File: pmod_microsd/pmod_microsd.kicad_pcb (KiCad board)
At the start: 2 copper layers, 11 parts, among them J1 PZ254R-12-12P, J2 Micro_SD_Card_Det2

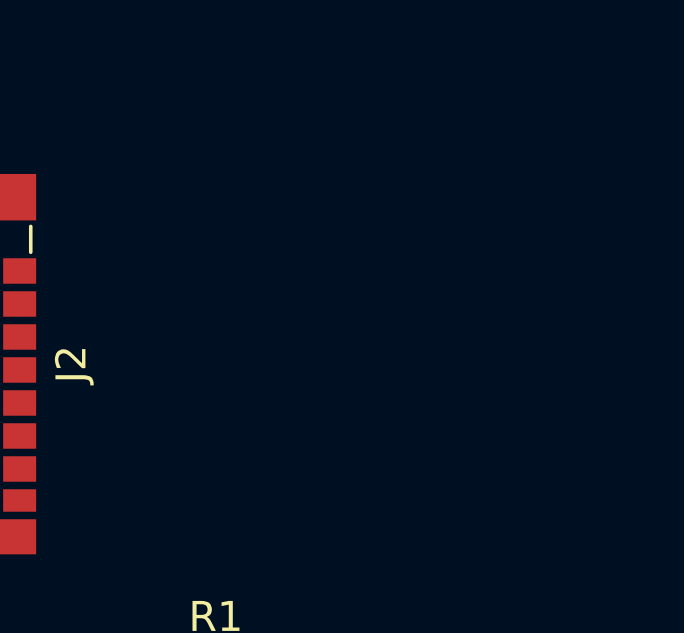
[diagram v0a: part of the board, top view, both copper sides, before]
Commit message: pmod_microsd/*.kicad_pcb: import schematic to pcb
- Import components from schematic to PCB

Signed-off-by: Huang Rui <vowstar@gmail.com>
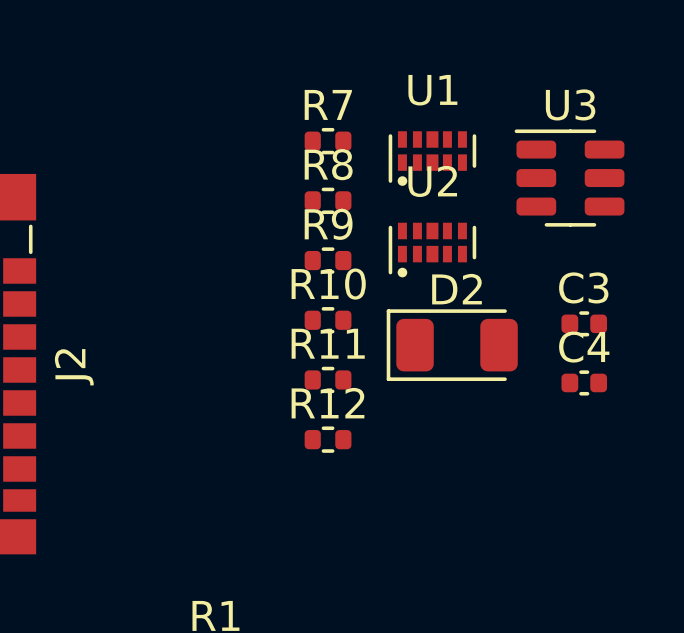
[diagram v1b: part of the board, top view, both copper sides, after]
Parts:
- added C3: 100n, Capacitor_SMD:C_0402_1005Metric, F.Cu at (134.0, 117.6)
- added C4: 100n, Capacitor_SMD:C_0402_1005Metric, F.Cu at (134.0, 119.6)
- added D2: NCD1206O1, LED_SMD:LED_1206_3216Metric, F.Cu at (129.8, 118.4)
- added R10: 10k, Resistor_SMD:R_0402_1005Metric, F.Cu at (125.5, 117.5)
- added R11: 6.8k, Resistor_SMD:R_0402_1005Metric, F.Cu at (125.5, 119.5)
- added R12: 6.8k, Resistor_SMD:R_0402_1005Metric, F.Cu at (125.5, 121.5)
- added R7: 330, Resistor_SMD:R_0402_1005Metric, F.Cu at (125.5, 111.6)
- added R8: 10k, Resistor_SMD:R_0402_1005Metric, F.Cu at (125.5, 113.5)
- added R9: 10k, Resistor_SMD:R_0402_1005Metric, F.Cu at (125.5, 115.5)
- added U1: RCLAMP0524P, CHIPSAlliance_Package_SON:USON-10_2.5x1.0mm_P0.5mm, F.Cu at (129.0, 111.9)
- added U2: RCLAMP0524P, CHIPSAlliance_Package_SON:USON-10_2.5x1.0mm_P0.5mm, F.Cu at (129.0, 114.9)
- added U3: AIP74LVC1T45GB236TR, Package_TO_SOT_SMD:SOT-23-6, F.Cu at (133.6, 112.8)
- C1, C2: value 100n -> 10u
- R1, R2: value 47k -> 200
- R3, R4, R5: value 47k -> 330
- R6: value 6.8k -> 330
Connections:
- C1 pad 1: VADJ -> 3P3V
- D1 pad 2: 3P3V -> Net-(D1-A)
- J1 pad 10: unconnected-(J1-Pin_10-Pad10) -> /SD_WP_PMOD
- J1 pad 9: /HVGPIO5 -> /SD_DET_PMOD
- J2 pad 10: Net-(J2-DET_A) -> /SD_DET
- R1 pad 1: /SD_DAT0 -> /SD_DET
- R1 pad 2: Net-(R1-Pad2) -> /SD_DET_PMOD
- R2 pad 1: /SD_DAT1 -> /SD_WP
- R2 pad 2: Net-(R1-Pad2) -> /SD_WP_PMOD
- R3 pad 1: /SD_DAT2 -> /SD_DAT0
- R3 pad 2: Net-(R1-Pad2) -> 3P3V
- R4 pad 1: /SD_DAT3 -> /SD_DAT1
- R4 pad 2: Net-(R1-Pad2) -> 3P3V
- R5 pad 1: /SD_CMD -> /SD_DAT2
- R5 pad 2: Net-(R1-Pad2) -> 3P3V
- R6 pad 1: Net-(J2-DET_A) -> /SD_DAT3
- R6 pad 2: Net-(D1-K) -> 3P3V

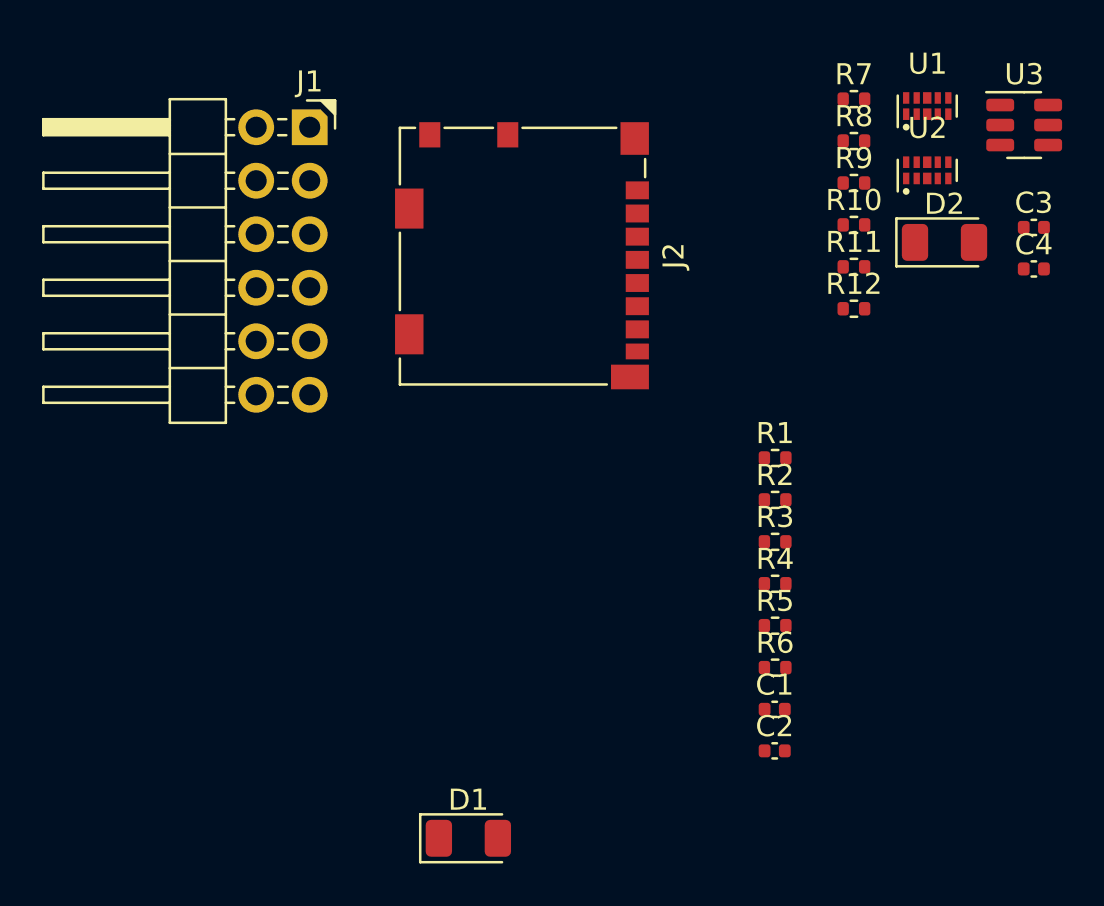
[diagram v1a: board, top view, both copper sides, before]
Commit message: pmod_microsd/*.kicad_pcb: draft placement
- Preliminary completion of component placement draft

Signed-off-by: Huang Rui <vowstar@gmail.com>
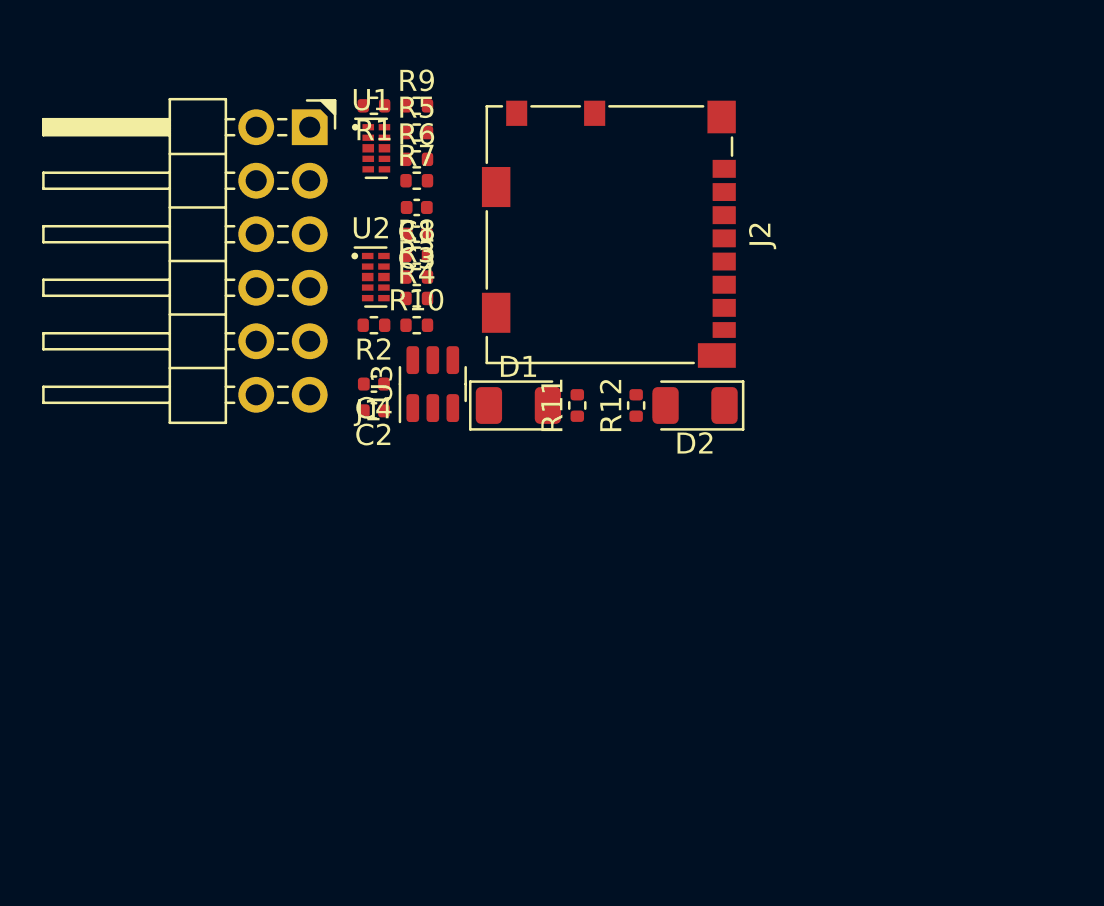
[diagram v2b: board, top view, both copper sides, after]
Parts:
- moved C4 31.8 mm to (102.7, 125.1), turned to 180 degrees
- moved U3 30.6 mm to (105.5, 125.1), turned to 90 degrees
- moved R6 29.5 mm to (104.7, 114.4)
- moved C3 29.3 mm to (104.7, 118.0), turned to 180 degrees
- moved C1 29.3 mm to (104.7, 116.7), turned to 180 degrees
- moved R5 28.9 mm to (104.7, 113.1)
- moved U2 26.7 mm to (102.8, 120.0), turned to -90 degrees
- moved U1 26.2 mm to (102.8, 113.9), turned to -90 degrees
- moved R1 25.3 mm to (102.7, 111.9), turned to 180 degrees
- moved C2 24.9 mm to (102.7, 126.4), turned to 180 degrees
- moved R4 21.7 mm to (104.7, 121.0)
- moved R8 21.5 mm to (104.7, 119.0)
- moved R10 21.3 mm to (104.7, 122.3)
- moved R3 21.1 mm to (104.7, 120.0)
- moved R7 21.1 mm to (104.7, 115.4)
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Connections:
- U1 pad 1: /SD_DAT3 -> /SD_DET_PMOD
- U1 pad 10: /SD_DAT3 -> /SD_DET_PMOD
- U1 pad 2: /SD_CMD -> /SD_DAT2
- U1 pad 4: /SD_DAT0 -> /SD_DAT3
- U1 pad 5: /SD_CLK -> /SD_CMD
- U1 pad 6: /SD_CLK -> /SD_CMD
- U1 pad 7: /SD_DAT0 -> /SD_DAT3
- U1 pad 9: /SD_CMD -> /SD_DAT2
- U2 pad 1: /SD_DAT1 -> /SD_CLK
- U2 pad 10: /SD_DAT1 -> /SD_CLK
- U2 pad 2: /SD_DAT2 -> /SD_DAT0
- U2 pad 4: /SD_DET_PMOD -> /SD_DAT1
- U2 pad 7: /SD_DET_PMOD -> /SD_DAT1
- U2 pad 9: /SD_DAT2 -> /SD_DAT0

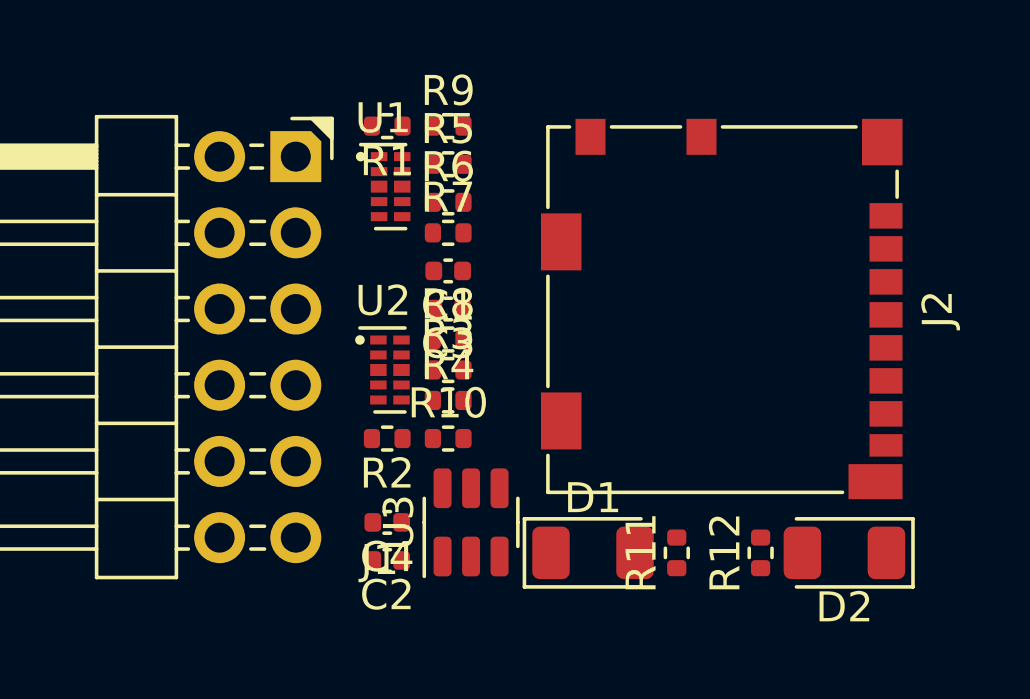
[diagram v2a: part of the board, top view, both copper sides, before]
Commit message: pmod_microsd/*.kicad_pcb: PCB outline definition
- Complete PCB outline and size definition
- Arrange silk screen
- Arrange text objects

Signed-off-by: Huang Rui <vowstar@gmail.com>
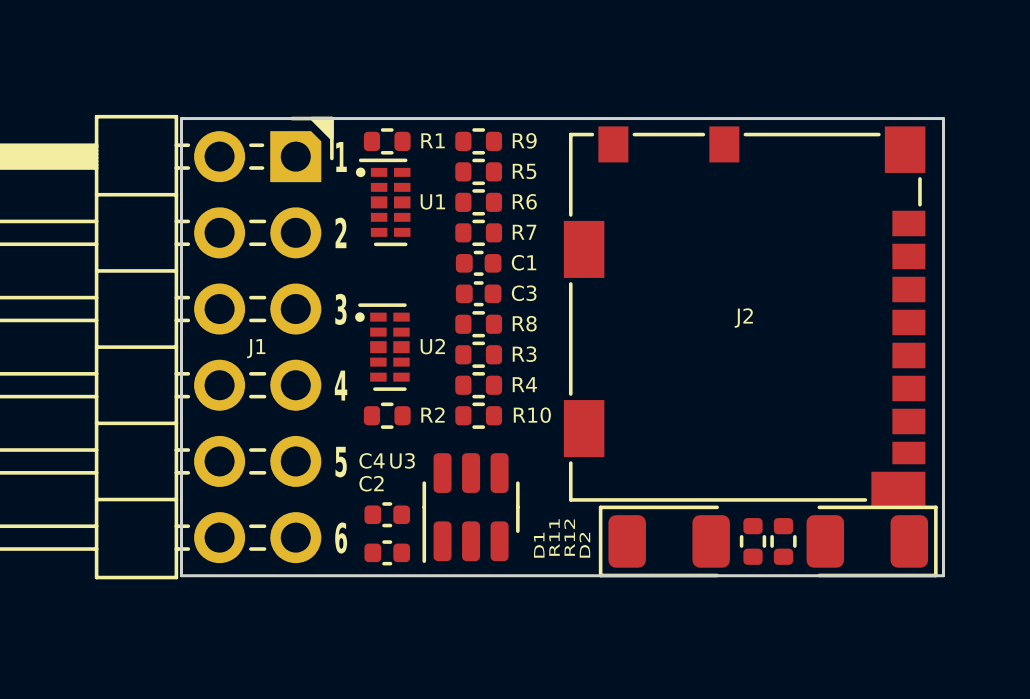
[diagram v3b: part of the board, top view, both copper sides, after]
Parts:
- moved D1 2.57 mm to (112.1, 125.7)
- moved R11 2.57 mm to (114.9, 125.7)
- moved R10 1.27 mm to (105.7, 121.5)
- moved R3 1.14 mm to (105.7, 119.5)
- moved C3 1.14 mm to (105.7, 117.5)
- moved R4 1.14 mm to (105.7, 120.5)
- moved R8 1.14 mm to (105.7, 118.5)
- moved R9 1.14 mm to (105.7, 112.4)
- moved C1 1.05 mm to (105.7, 116.4)
- moved R5 1.05 mm to (105.7, 113.4)
- moved R6 1.02 mm to (105.7, 114.4)
- moved R7 1.02 mm to (105.7, 115.4)
- moved D2 0.85 mm to (118.7, 125.7)
- moved R12 0.85 mm to (115.9, 125.7)
- moved J2 0.80 mm to (114.6, 118.2)
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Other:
- board outline added: 25.4 x 15.2 mm
- board text added: "1"
- board text added: "2"
- board text added: "3"
- board text added: "4"
- board text added: "5"
- board text added: "6"

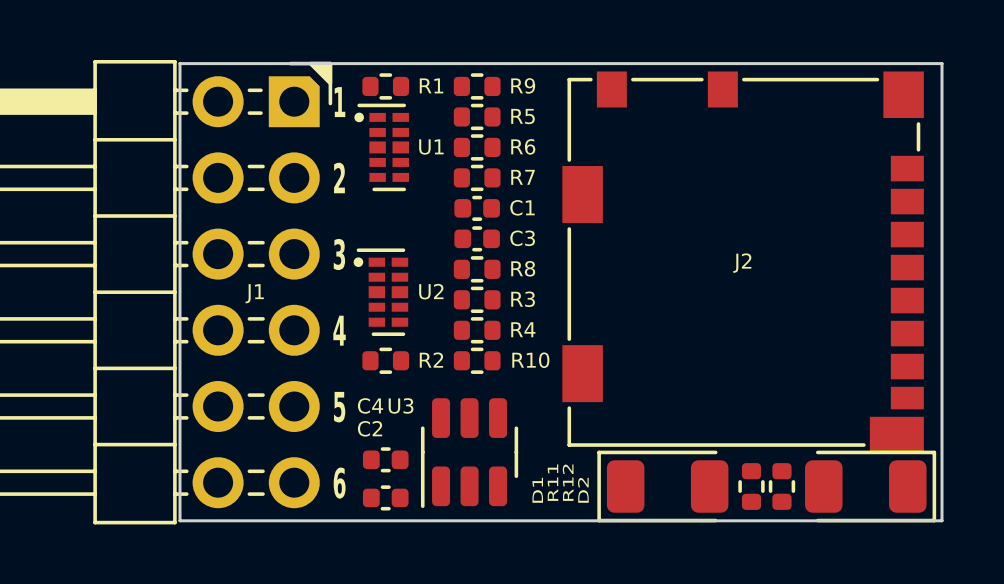
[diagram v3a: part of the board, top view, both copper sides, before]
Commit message: pmod_microsd/*.kicad_pcb: Complete PCB layout and routing
- Complete PCB layout
- Complete PCB routing
- Complete PCB silk screen placement
- LVS comparison successful
- DRC cleared

Signed-off-by: Huang Rui <vowstar@gmail.com>
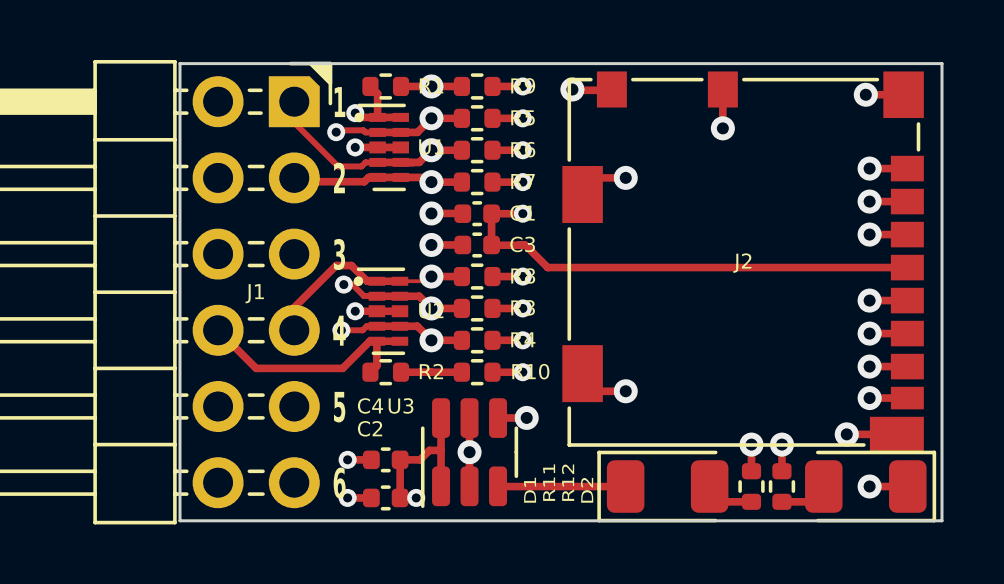
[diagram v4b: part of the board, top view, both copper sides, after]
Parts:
- moved U2 0.63 mm to (102.8, 119.9)
- moved R10 0.38 mm to (105.7, 121.9)
- moved R2 0.38 mm to (102.7, 121.9)
- moved R4 0.33 mm to (105.7, 120.8)
- moved R3 0.29 mm to (105.7, 119.8)
- moved R8 0.24 mm to (105.7, 118.7)
- moved C3 0.20 mm to (105.7, 117.7)
- moved C1 0.18 mm to (105.7, 116.6)
- moved R7 0.14 mm to (105.7, 115.6)
- moved R6 0.09 mm to (105.7, 114.5)
- turned R11 to -90 degrees
- turned R12 to -90 degrees
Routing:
- net 3P3V: track 0.00 -> 31.9 mm, vias 0 -> 12
- net /SD_DAT1: track 0.00 -> 30.7 mm, vias 0 -> 3
- net /SD_DAT2: track 0.00 -> 25.4 mm, vias 0 -> 3
- net /SD_DET: track 0.00 -> 24.6 mm, vias 0 -> 3
- net /SD_DAT3: track 0.00 -> 24.2 mm, vias 0 -> 2
- net /SD_CLK: track 0.00 -> 23.4 mm, vias 0 -> 2
- net /SD_DAT0: track 0.00 -> 23.0 mm, vias 0 -> 3
- net /SD_CMD: track 0.00 -> 22.4 mm, vias 0 -> 2
- net GND: track 0.00 -> 19.1 mm, vias 0 -> 14
- net /SD_DET_PMOD: track 0.00 -> 11.2 mm, vias 0 -> 1
- net /SD_WP_PMOD: track 0.00 -> 8.09 mm
- net Net-(D1-K): track 0.00 -> 4.26 mm
- net /SD_WP: track 0.00 -> 2.03 mm
- net Net-(D2-A): track 0.00 -> 1.61 mm
- net Net-(D1-A): track 0.00 -> 1.61 mm
- added copper zone on In2.Cu, net 3P3V
- added copper zone on B.Cu, net GND
- added copper zone on F.Cu, net GND
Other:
- copper layers 2 -> 4
- board text added: "CLK"
- board text added: "CMD"
- board text added: "D0"
- board text added: "D1"
- board text added: "D2"
- board text added: "D3"
- board text added: "GND"
- board text added: "PMOD_MICROSD Rev: ${REVISION} 6buE6ZSQ By: Rui Huang Date: ${ISSUE_DATE}"
- board text added: "VDD"
- board text added: "~{CD}"
- board text added: "~{WP}"

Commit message: pmod_microsd:*.kicad_pcb: add board characteristics
- Add board stackup table
- Add board characteristics

Signed-off-by: Huang Rui <vowstar@gmail.com>
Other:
- board text added: "0"
- board text added: "0 mm"
- board text added: "0.01 mm"
- board text added: "0.02"
- board text added: "0.035 mm"
- board text added: "0.1 mm"
- board text added: "0.1270 mm / 0.1270 mm"
- board text added: "0.3000 mm"
- board text added: "1.257 mm"
- board text added: "1.6170 mm"
- board text added: "2313"
- board text added: "25.4000 mm x 15.2400 mm"
- board text added: "3.3"
- board text added: "4.05"
- board text added: "4.5"
- board text added: "B.Cu"
- board text added: "B.Mask"
- board text added: "B.Paste"
- board text added: "B.Silkscreen"
- board text added: "BOARD CHARACTERISTICS"
- board text added: "Black"
- board text added: "Board Thickness:"
- board text added: "Board overall dimensions:"
- board text added: "Bottom Silk Screen"
- board text added: "Bottom Solder Mask"
- board text added: "Bottom Solder Paste"
- board text added: "Castellated pads:"
- board text added: "Color"
- board text added: "Copper Finish:"
- board text added: "Copper Layer Count:"
- board text added: "Dielectric"
- board text added: "Edge card connectors:"
- board text added: "Epsilon R"
- board text added: "F.Cu"
- board text added: "F.Mask"
- board text added: "F.Paste"
- board text added: "F.Silkscreen"
- board text added: "FR4"
- board text added: "Impedance Control:"
- board text added: "In1.Cu"
- board text added: "In2.Cu"
- board text added: "Layer Name"
- board text added: "Loss Tangent"
- board text added: "Material"
- board text added: "Min hole diameter:"
- board text added: "Min track/spacing:"
- board text added: "No"
- board text added: "None"
- board text added: "Not specified"
- board text added: "Plated Board Edge:"
- board text added: "Thickness (mm)"
- board text added: "Top Silk Screen"
- board text added: "Top Solder Mask"
- board text added: "Top Solder Paste"
- board text added: "Type"
- board text added: "White"
- board text added: "copper"
- board text added: "core"
- board text added: "prepreg"
